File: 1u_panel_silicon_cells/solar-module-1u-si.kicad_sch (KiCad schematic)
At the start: 6 parts

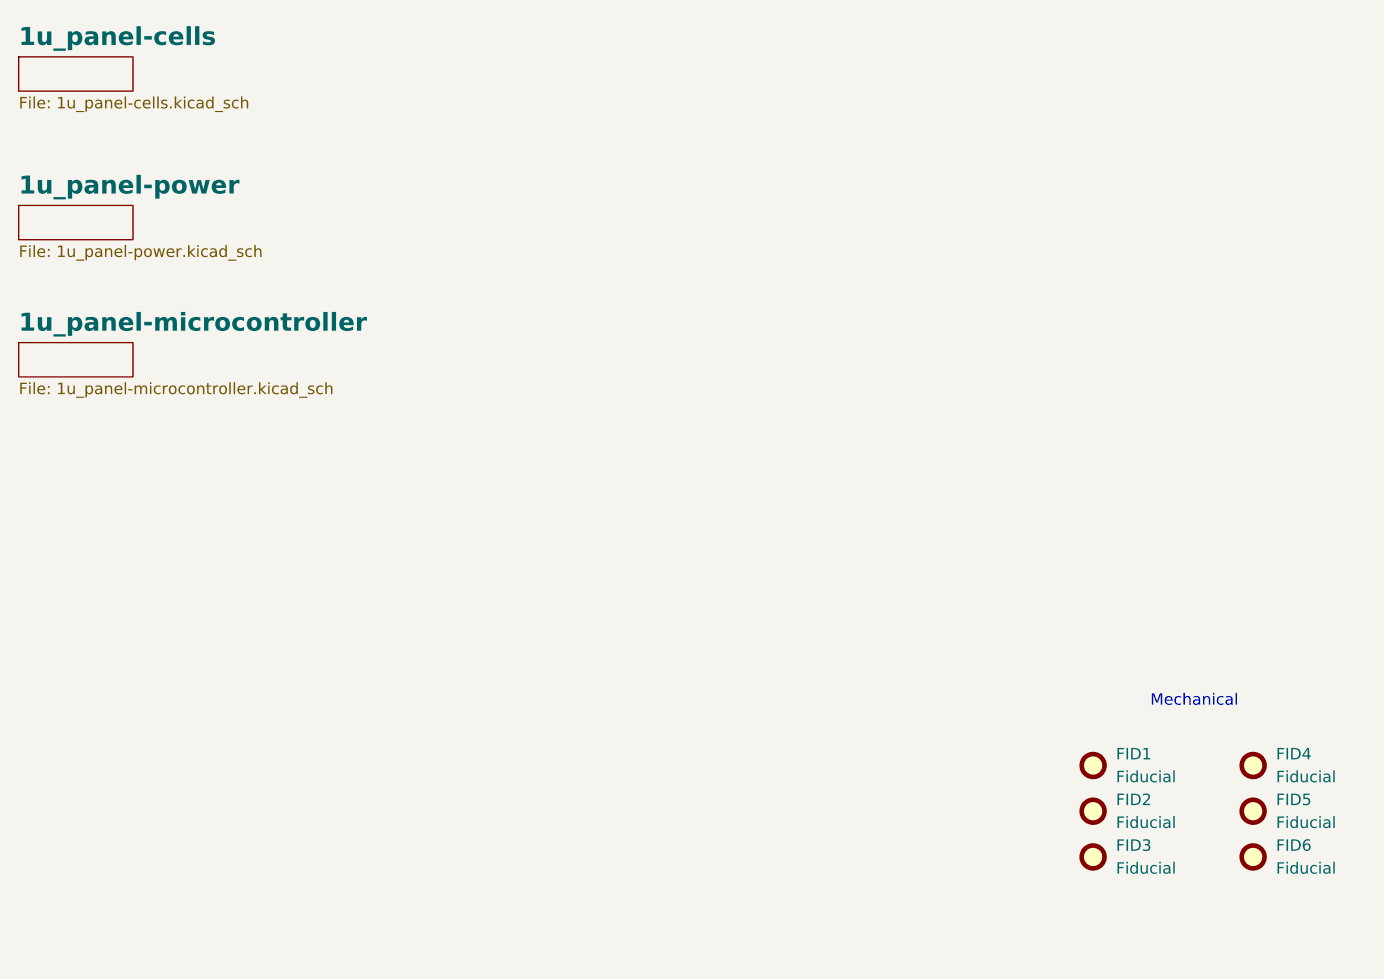
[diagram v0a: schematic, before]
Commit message: Yeah, renamed everything because consistancy.
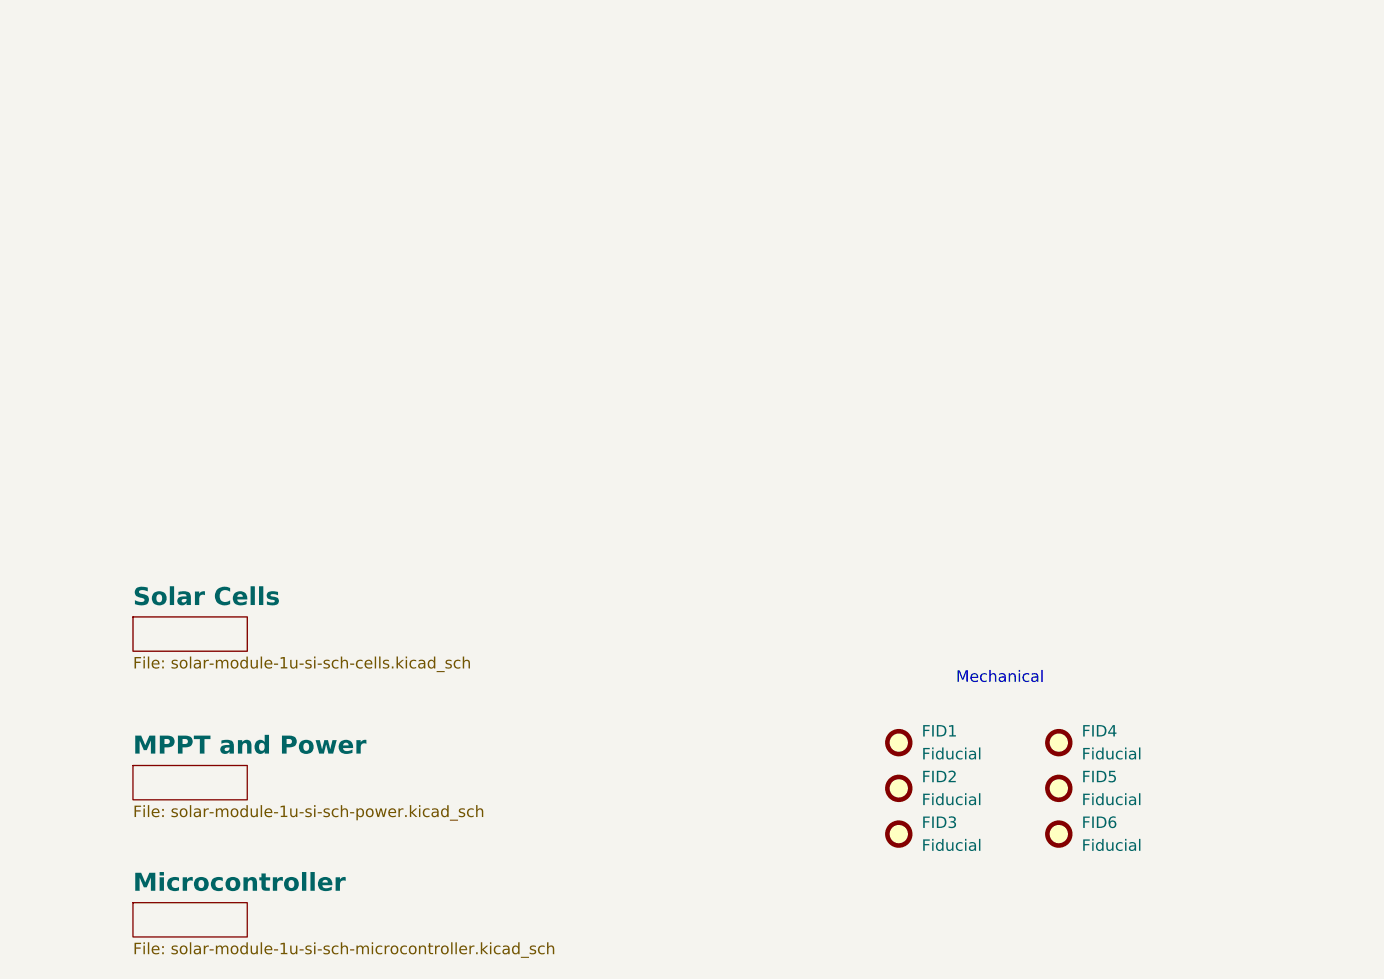
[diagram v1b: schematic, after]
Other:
- sheet 1u_panel-cells renamed Solar Cells
- sheet 1u_panel-microcontroller renamed Microcontroller
- sheet 1u_panel-power renamed MPPT and Power
- sheet MPPT and Power: file 1u_panel-power.kicad_sch -> solar-module-1u-si-sch-power.kicad_sch
- sheet Microcontroller: file 1u_panel-microcontroller.kicad_sch -> solar-module-1u-si-sch-microcontroller.kicad_sch
- sheet Solar Cells: file 1u_panel-cells.kicad_sch -> solar-module-1u-si-sch-cells.kicad_sch
- moved on the sheet: FID1, FID2, FID3, FID4, FID5, FID6
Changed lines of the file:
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@@
 	(text "Mechanical"
 		(exclude_from_sim no)
-		(at 161.29 111.76 0)
+		(at 139.7 109.22 0)
 		(effects
 			(font
@@
 	(symbol
 		(lib_id "Mechanical:Fiducial")
-		(at 154.94 123.19 0)
+		(at 133.35 120.65 0)
 		(unit 1)
 		(exclude_from_sim no)
@@
 		(fields_autoplaced yes)
 		(property "Reference" "FID2"
-			(at 157.48 121.9199 0)
+			(at 135.89 119.3799 0)
 			(effects
 				(font
@@
 		)
 		(property "Value" "Fiducial"
-			(at 157.48 124.4599 0)
+			(at 135.89 121.9199 0)
 			(effects
 				(font
@@
 		)
 		(property "Footprint" "Fiducial:Fiducial_1mm_Mask2mm"
-			(at 154.94 123.19 0)
+			(at 133.35 120.65 0)
 			(effects
 				(font
@@
 		)
 		(property "Datasheet" "~"
-			(at 154.94 123.19 0)
+			(at 133.35 120.65 0)
 			(effects
 				(font
@@
 		)
 		(property "Description" "Fiducial Marker"
-			(at 154.94 123.19 0)
+			(at 133.35 120.65 0)
 			(effects
 				(font
@@
 	(symbol
 		(lib_id "Mechanical:Fiducial")
-		(at 172.72 123.19 0)
+		(at 151.13 120.65 0)
 		(unit 1)
 		(exclude_from_sim no)
@@
 		(fields_autoplaced yes)
 		(property "Reference" "FID5"
-			(at 175.26 121.9199 0)
+			(at 153.67 119.3799 0)
 			(effects
 				(font
@@
 		)
 		(property "Value" "Fiducial"
-			(at 175.26 124.4599 0)
+			(at 153.67 121.9199 0)
 			(effects
 				(font
@@
 		)
 		(property "Footprint" "Fiducial:Fiducial_1mm_Mask2mm"
-			(at 172.72 123.19 0)
+			(at 151.13 120.65 0)
 			(effects
 				(font
@@
 		)
 		(property "Datasheet" "~"
-			(at 172.72 123.19 0)
+			(at 151.13 120.65 0)
 			(effects
 				(font
@@
 		)
 		(property "Description" "Fiducial Marker"
-			(at 172.72 123.19 0)
+			(at 151.13 120.65 0)
 			(effects
 				(font
@@
 	(symbol
 		(lib_id "Mechanical:Fiducial")
-		(at 154.94 128.27 0)
+		(at 133.35 125.73 0)
 		(unit 1)
 		(exclude_from_sim no)
@@
 		(fields_autoplaced yes)
 		(property "Reference" "FID3"
-			(at 157.48 126.9999 0)
+			(at 135.89 124.4599 0)
 			(effects
 				(font
@@
 		)
 		(property "Value" "Fiducial"
-			(at 157.48 129.5399 0)
+			(at 135.89 126.9999 0)
 			(effects
 				(font
@@
 		)
 		(property "Footprint" "Fiducial:Fiducial_1mm_Mask2mm"
-			(at 154.94 128.27 0)
+			(at 133.35 125.73 0)
 			(effects
 				(font
@@
 		)
 		(property "Datasheet" "~"
-			(at 154.94 128.27 0)
+			(at 133.35 125.73 0)
 			(effects
 				(font
@@
 		)
 		(property "Description" "Fiducial Marker"
-			(at 154.94 128.27 0)
+			(at 133.35 125.73 0)
 			(effects
 				(font
@@
 	(symbol
 		(lib_id "Mechanical:Fiducial")
-		(at 172.72 118.11 0)
+		(at 151.13 115.57 0)
 		(unit 1)
 		(exclude_from_sim no)
@@
 		(fields_autoplaced yes)
 		(property "Reference" "FID4"
-			(at 175.26 116.8399 0)
+			(at 153.67 114.2999 0)
 			(effects
 				(font
@@
 		)
 		(property "Value" "Fiducial"
-			(at 175.26 119.3799 0)
+			(at 153.67 116.8399 0)
 			(effects
 				(font
@@
 		)
 		(property "Footprint" "Fiducial:Fiducial_1mm_Mask2mm"
-			(at 172.72 118.11 0)
+			(at 151.13 115.57 0)
 			(effects
 				(font
@@
 		)
 		(property "Datasheet" "~"
-			(at 172.72 118.11 0)
+			(at 151.13 115.57 0)
 			(effects
 				(font
@@
 		)
 		(property "Description" "Fiducial Marker"
-			(at 172.72 118.11 0)
+			(at 151.13 115.57 0)
 			(effects
 				(font
@@
 	(symbol
 		(lib_id "Mechanical:Fiducial")
-		(at 154.94 118.11 0)
+		(at 133.35 115.57 0)
 		(unit 1)
 		(exclude_from_sim no)
@@
 		(fields_autoplaced yes)
 		(property "Reference" "FID1"
-			(at 157.48 116.8399 0)
+			(at 135.89 114.2999 0)
 			(effects
 				(font
@@
 		)
 		(property "Value" "Fiducial"
-			(at 157.48 119.3799 0)
+			(at 135.89 116.8399 0)
 			(effects
 				(font
@@
 		)
 		(property "Footprint" "Fiducial:Fiducial_1mm_Mask2mm"
-			(at 154.94 118.11 0)
+			(at 133.35 115.57 0)
 			(effects
 				(font
@@
 		)
 		(property "Datasheet" "~"
-			(at 154.94 118.11 0)
+			(at 133.35 115.57 0)
 			(effects
 				(font
@@
 		)
 		(property "Description" "Fiducial Marker"
-			(at 154.94 118.11 0)
+			(at 133.35 115.57 0)
 			(effects
 				(font
@@
 	(symbol
 		(lib_id "Mechanical:Fiducial")
-		(at 172.72 128.27 0)
+		(at 151.13 125.73 0)
 		(unit 1)
 		(exclude_from_sim no)
@@
 		(fields_autoplaced yes)
 		(property "Reference" "FID6"
-			(at 175.26 126.9999 0)
+			(at 153.67 124.4599 0)
 			(effects
 				(font
@@
 		)
 		(property "Value" "Fiducial"
-			(at 175.26 129.5399 0)
+			(at 153.67 126.9999 0)
 			(effects
 				(font
@@
 		)
 		(property "Footprint" "Fiducial:Fiducial_1mm_Mask2mm"
-			(at 172.72 128.27 0)
+			(at 151.13 125.73 0)
 			(effects
 				(font
@@
 		)
 		(property "Datasheet" "~"
-			(at 172.72 128.27 0)
+			(at 151.13 125.73 0)
 			(effects
 				(font
@@
 		)
 		(property "Description" "Fiducial Marker"
-			(at 172.72 128.27 0)
+			(at 151.13 125.73 0)
 			(effects
 				(font
@@
 	)
 	(sheet
-		(at 35.56 55.88)
+		(at 48.26 118.11)
 		(size 12.7 3.81)
 		(exclude_from_sim no)
@@
 			(color 0 0 0 0.0000)
 		)
-		(property "Sheetname" "1u_panel-power"
-			(at 35.56 54.8034 0)
+		(property "Sheetname" "MPPT and Power"
+			(at 48.26 117.0334 0)
 			(effects
 				(font
@@
 			)
 		)
-		(property "Sheetfile" "1u_panel-power.kicad_sch"
-			(at 35.56 60.2746 0)
+		(property "Sheetfile" "solar-module-1u-si-sch-power.kicad_sch"
+			(at 48.26 122.5046 0)
 			(effects
 				(font
@@
 		)
 		(instances
-			(project "1u_panel-silicon"
+			(project "solar-module-1u-si"
 				(path "/115bd2cd-7c08-4b54-867b-a326ee0699c1"
 					(page "2")
@@
 	)
 	(sheet
-		(at 35.56 71.12)
+		(at 48.26 133.35)
 		(size 12.7 3.81)
 		(exclude_from_sim no)
@@
 			(color 0 0 0 0.0000)
 		)
-		(property "Sheetname" "1u_panel-microcontroller"
-			(at 35.56 70.0434 0)
+		(property "Sheetname" "Microcontroller"
+			(at 48.26 132.2734 0)
 			(effects
 				(font
@@
 			)
 		)
-		(property "Sheetfile" "1u_panel-microcontroller.kicad_sch"
-			(at 35.56 75.5146 0)
+		(property "Sheetfile" "solar-module-1u-si-sch-microcontroller.kicad_sch"
+			(at 48.26 137.7446 0)
 			(effects
 				(font
@@
 		)
 		(instances
-			(project "1u_panel-silicon"
+			(project "solar-module-1u-si"
 				(path "/115bd2cd-7c08-4b54-867b-a326ee0699c1"
 					(page "3")
@@
 	)
 	(sheet
-		(at 35.56 39.37)
+		(at 48.26 101.6)
 		(size 12.7 3.81)
 		(exclude_from_sim no)
@@
 			(color 0 0 0 0.0000)
 		)
-		(property "Sheetname" "1u_panel-cells"
-			(at 35.56 38.2934 0)
+		(property "Sheetname" "Solar Cells"
+			(at 48.26 100.5234 0)
 			(effects
 				(font
@@
 			)
 		)
-		(property "Sheetfile" "1u_panel-cells.kicad_sch"
-			(at 35.56 43.7646 0)
+		(property "Sheetfile" "solar-module-1u-si-sch-cells.kicad_sch"
+			(at 48.26 105.9946 0)
 			(effects
 				(font
@@
 		)
 		(instances
-			(project "1u_panel-silicon"
+			(project "solar-module-1u-si"
 				(path "/115bd2cd-7c08-4b54-867b-a326ee0699c1"
 					(page "1")
